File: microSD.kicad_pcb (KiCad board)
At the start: 16 copper layers, 31.8 x 25.4 mm, 14 parts, among them IC1 4050D, IC2 LP298XS, X1 MICROSD

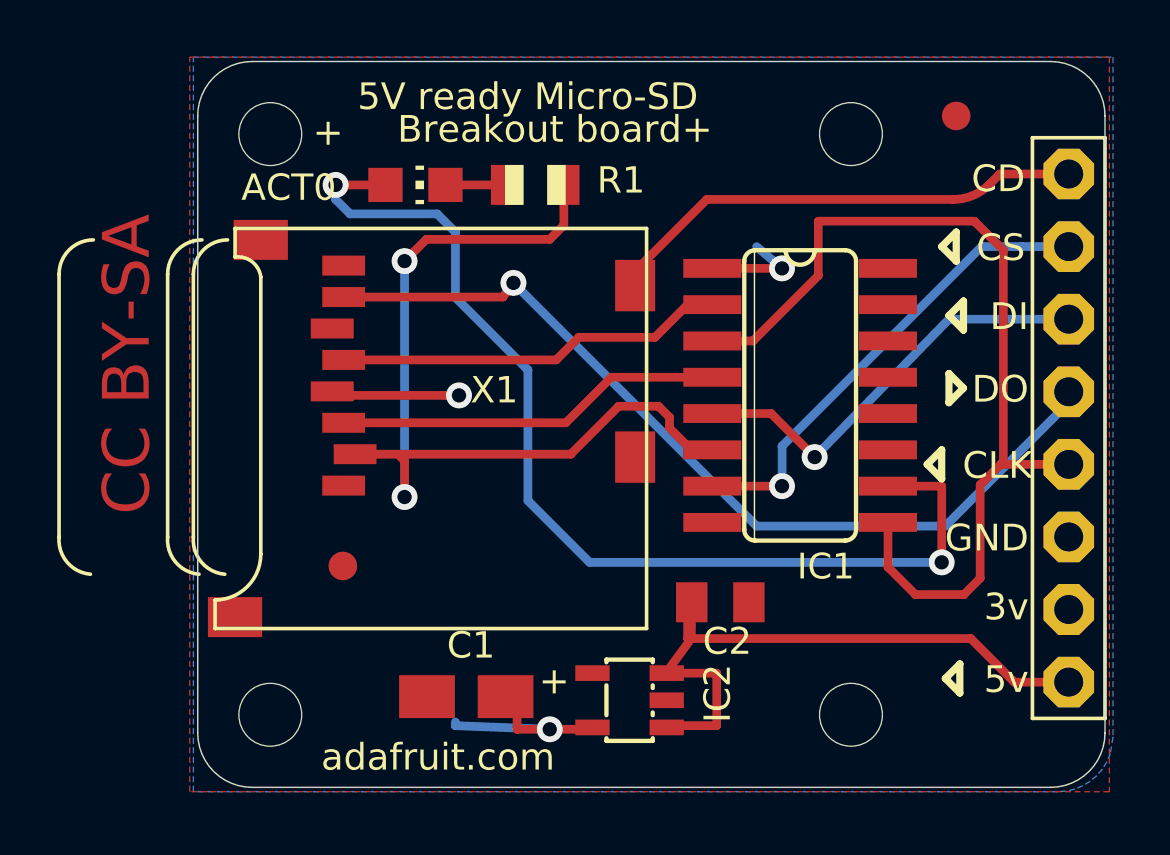
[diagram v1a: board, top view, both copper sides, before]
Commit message: fully migrated to KiCad
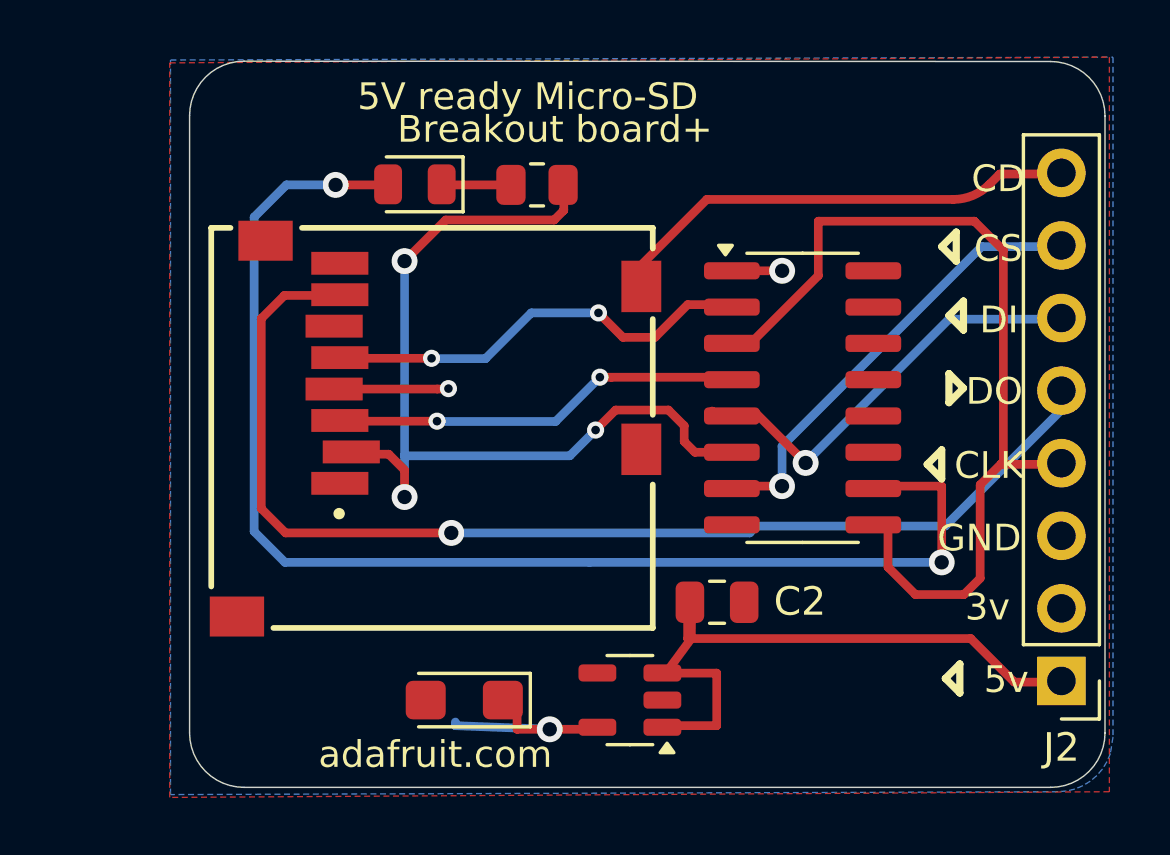
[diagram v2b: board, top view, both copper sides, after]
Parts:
- removed @HOLE0, @HOLE1, @HOLE2, @HOLE3: , 
- removed U$1, U$2: FIDUCIAL, FIDUCIAL_1MM
- C1: footprint A_3216-18R -> Capacitor_Tantalum_SMD:CP_EIA-3216-18_Kemet-A
- C2: footprint C0805K -> Capacitor_SMD:C_0805_2012Metric
- D1: renamed from ACT0; footprint CHIP-LED0805 -> LED_SMD:LED_0805_2012Metric
- IC1: value 4050D -> ~; footprint SO16 -> Package_SO:SOIC-16_3.9x9.9mm_P1.27mm
- IC2: footprint SOT23-5L -> Package_TO_SOT_SMD:SOT-23-5
- J1: renamed from X1; value MICROSD -> Micro_SD_Card_Det2; footprint MICROSD -> external_footprints:GCT_MEM2061-01-188-00-A_REVA
- J2: renamed from JP1; value (none) -> PINHD-1X8BIG; footprint 1X08-BIG -> Connector_PinHeader_2.54mm:PinHeader_1x08_P2.54mm_Vertical
- R1: footprint R0805 -> Resistor_SMD:R_0805_2012Metric
- moved J1 10.3 mm to (140.8, 105.1)
- moved J2 8.85 mm to (162.8, 114.0), turned to 180 degrees
- moved C1 0.14 mm to (142.0, 114.7), turned to 180 degrees
- moved IC1 0.12 mm to (153.8, 104.1), turned to 0 degrees
- moved C2 0.11 mm to (150.8, 111.2)
- moved R1 0.06 mm to (144.5, 96.6)
- turned D1 to 180 degrees
- turned IC2 to 180 degrees
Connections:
- net CLK renamed /CLK
- net CS renamed /CS
- net DI renamed /DI
- net DO renamed /DO
- net N$2 renamed /1Y
- net N$3 renamed /3Y
- net N$5 renamed /2Y
- IC1 pad 1: +3V3 -> +3.3V
- IC1 pad 10: N$1 -> /4Y
- IC1 pad 12: (no net) -> unconnected-(IC1-5Y-Pad12)
- IC1 pad 13: (no net) -> unconnected-(IC1-NC-Pad13)
- IC1 pad 15: (no net) -> unconnected-(IC1-6Y-Pad15)
- IC1 pad 16: (no net) -> unconnected-(IC1-NC-Pad16)
- IC2 pad 4: (no net) -> unconnected-(IC2-BYP-Pad4)
- IC2 pad 5: +3V3 -> +3.3V
- J1 pad 1: (no net) -> unconnected-(J1-DAT2-Pad1)
- J1 pad 4: +3V3 -> +3.3V
- J1 pad 8: (no net) -> unconnected-(J1-DAT1-Pad8)
- J2 pad 2: +3V3 -> +3.3V
- J2 pad 8: CD -> /CD
- R1 pad 2: N$4 -> Net-(D1-K)
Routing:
- net /4Y: track 0.00 -> 45.1 mm, vias 0 -> 2
- net N$1: track 37.3 -> 0.00 mm, vias 2 -> 0
- net CD: track 18.0 -> 0.00 mm
- net /CD: track 0.00 -> 18.0 mm
- net +3V3: track 16.4 -> 0.00 mm, vias 3 -> 0
- net +3.3V: track 0.00 -> 13.5 mm, vias 0 -> 3
- net /DO: track 31.7 -> 40.8 mm
- net Net-(D1-K): track 0.00 -> 2.31 mm
- net N$4: track 2.31 -> 0.00 mm
- net /1Y: track 13.9 -> 14.9 mm, vias 0 -> 2
- net /3Y: track 31.8 -> 31.4 mm, vias 2 -> 3
- net /2Y: track 13.6 -> 13.9 mm, vias 0 -> 2
- added copper zone on B.Cu, net +3.3V
- removed copper zone on B.Cu, net +3V3
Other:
- board size 31.8 x 25.4 mm -> 32 x 25.4 mm
- board text removed: "CC BY-SA"

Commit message: added info to generate BOM file
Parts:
- C1: value 10uF/10V -> 10uF; footprint Capacitor_Tantalum_SMD:CP_EIA-3216-18_Kemet-A -> Capacitor_SMD:C_0805_2012Metric
- IC1: value ~ -> 74HC4050D
- IC2: value LP298XS -> LP2985A
- J1: value Micro_SD_Card_Det2 -> ~
- J2: value PINHD-1X8BIG -> ~
- R1: value 1K -> 1k
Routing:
- net +3.3V: track 13.5 -> 9.80 mm

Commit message: minor fixes schematic and PCB
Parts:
- J1: value ~ -> microSD
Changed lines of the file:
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@@
 			)
 		)
-		(property "Value" "~"
+		(property "Value" "microSD"
 			(at 20.95407 9.036605 90)
 			(layer "F.Fab")
@@
 			(layer "F.Fab")
 		)
+		(pad "" smd rect
+			(at 6.6 6.825 270)
+			(size 1.4 1.9)
+			(layers "F.Cu" "F.Paste" "F.Mask")
+			(solder_mask_margin 0.102)
+		)
 		(pad "1" smd rect
 			(at 1.94 3.225 270)
@@
 			(pinfunction "SHIELD")
 			(pintype "passive")
-			(solder_mask_margin 0.102)
-		)
-		(pad "12" smd rect
-			(at 6.6 6.825 270)
-			(size 1.4 1.9)
-			(layers "F.Cu" "F.Paste" "F.Mask")
 			(solder_mask_margin 0.102)
 		)
@@
 			(net 8 "unconnected-(IC1-NC-Pad13)")
 			(pinfunction "NC")
-			(pintype "no_connect")
+			(pintype "passive+no_connect")
 		)
 		(pad "14" smd roundrect
@@
 			(net 5 "unconnected-(IC1-NC-Pad16)")
 			(pinfunction "NC")
-			(pintype "no_connect")
+			(pintype "passive+no_connect")
 		)
 		(model "${KICAD8_3DMODEL_DIR}/Package_SO.3dshapes/SOIC-16_3.9x9.9mm_P1.27mm.wrl"
@@
 		(model "${KICAD8_3DMODEL_DIR}/Connector_PinHeader_2.54mm.3dshapes/PinHeader_1x08_P2.54mm_Vertical.wrl"
 			(offset
-				(xyz 0 0 2.5)
+				(xyz 0 0 -1.5)
 			)
 			(scale

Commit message: silkscreen update
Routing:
- net VCC: track 23.5 -> 21.6 mm
- net /CD: track 18.0 -> 17.2 mm
- net /CLK: track 33.3 -> 32.8 mm
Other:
- board text added: "microSD"
- board text removed: "5V ready Micro-SD"
- board text removed: "Breakout board+"
- board text removed: "adafruit.com"

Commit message: silkscreen + BOM update
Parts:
- added G***: LOGO, external_footprints:logo, F.Cu at (155.5, 113.6)

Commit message: removed unused copper layers
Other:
- copper layers 16 -> 2
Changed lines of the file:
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@@
 	(layers
 		(0 "F.Cu" signal)
-		(1 "In1.Cu" signal)
-		(2 "In2.Cu" signal)
-		(3 "In3.Cu" signal)
-		(4 "In4.Cu" signal)
-		(5 "In5.Cu" signal)
-		(6 "In6.Cu" signal)
-		(7 "In7.Cu" signal)
-		(8 "In8.Cu" signal)
-		(9 "In9.Cu" signal)
-		(10 "In10.Cu" signal)
-		(11 "In11.Cu" signal)
-		(12 "In12.Cu" signal)
-		(13 "In13.Cu" signal)
-		(14 "In14.Cu" signal)
 		(31 "B.Cu" signal)
 		(32 "B.Adhes" user "B.Adhesive")
@@
 	)
 	(setup
+		(stackup
+			(layer "F.SilkS"
+				(type "Top Silk Screen")
+			)
+			(layer "F.Paste"
+				(type "Top Solder Paste")
+			)
+			(layer "F.Mask"
+				(type "Top Solder Mask")
+				(thickness 0.01)
+			)
+			(layer "F.Cu"
+				(type "copper")
+				(thickness 0.035)
+			)
+			(layer "dielectric 1"
+				(type "core")
+				(thickness 1.51)
+				(material "FR4")
+				(epsilon_r 4.5)
+				(loss_tangent 0.02)
+			)
+			(layer "B.Cu"
+				(type "copper")
+				(thickness 0.035)
+			)
+			(layer "B.Mask"
+				(type "Bottom Solder Mask")
+				(thickness 0.01)
+			)
+			(layer "B.Paste"
+				(type "Bottom Solder Paste")
+			)
+			(layer "B.SilkS"
+				(type "Bottom Silk Screen")
+			)
+			(copper_finish "None")
+			(dielectric_constraints no)
+		)
 		(pad_to_mask_clearance 0)
 		(allow_soldermask_bridges_in_footprints no)
